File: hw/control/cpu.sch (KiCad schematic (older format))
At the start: 22 parts, among them J301 Conn_02x05_Odd_Even, J302 Conn_01x04, J303 Raspberry_Pi_0_2_3, J304 Micro_SD_Card, J305 Conn_01x06, J306 Conn_01x07, SW301 SW_Push

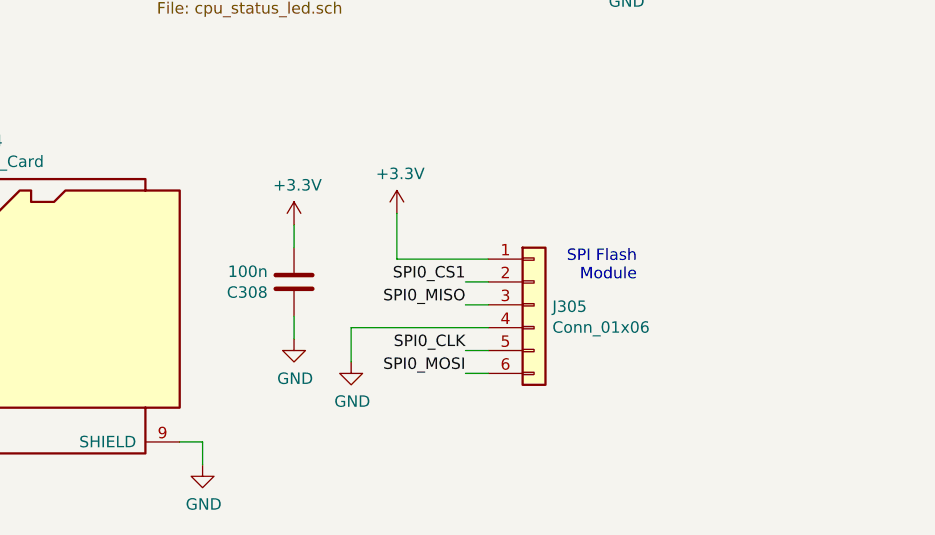
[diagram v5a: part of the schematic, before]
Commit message: [hw] Isolate SD card holder shield from ground
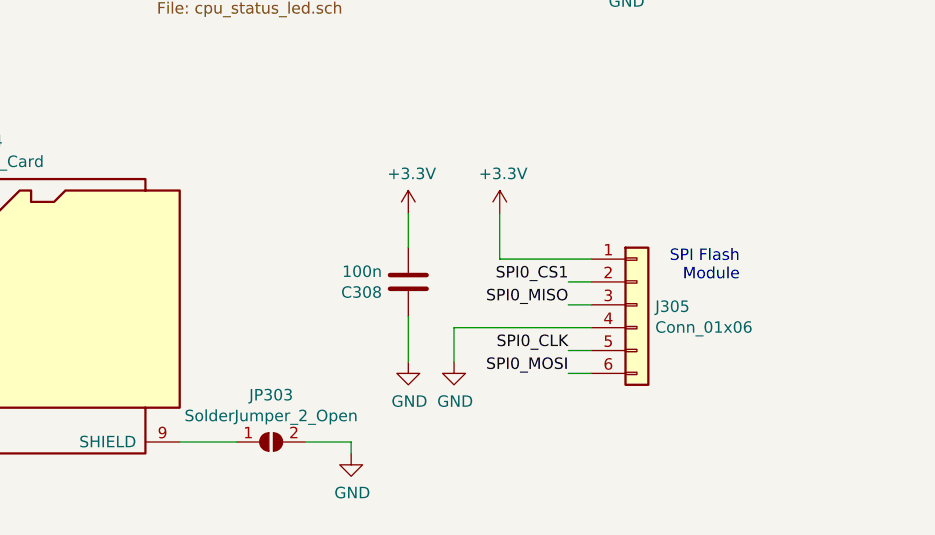
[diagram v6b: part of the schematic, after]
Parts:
- added JP303: SolderJumper_2_Open, Jumper:SolderJumper-2_P1.3mm_Open_RoundedPad1.0x1.5mm, symbol Jumper:SolderJumper_2_Open
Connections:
- net GND: now also JP303.2 (B); no longer J304.9 (SHIELD)
- new net: J304.9 (SHIELD), JP303.1 (A)
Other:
- moved on the sheet: C308, J305
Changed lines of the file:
@@
 L power:GND #PWR0322
 U 1 1 614D2941
-P 4100 7400
-F 0 "#PWR0322" H 4100 7150 50  0001 C CNN
-F 1 "GND" H 4105 7227 50  0000 C CNN
-F 2 "" H 4100 7400 50  0001 C CNN
-F 3 "" H 4100 7400 50  0001 C CNN
-	1    4100 7400
-	1    0    0    -1
-$EndComp
-Wire Wire Line
-	4000 7300 4100 7300
-Wire Wire Line
-	4100 7300 4100 7400
+P 4750 7350
+F 0 "#PWR0322" H 4750 7100 50  0001 C CNN
+F 1 "GND" H 4755 7177 50  0000 C CNN
+F 2 "" H 4750 7350 50  0001 C CNN
+F 3 "" H 4750 7350 50  0001 C CNN
+	1    4750 7350
+	1    0    0    -1
+$EndComp
 $Comp
 L Device:C C302
@@
 L power:+3.3V #PWR0317
 U 1 1 6164D788
-P 4950 6300
-F 0 "#PWR0317" H 4950 6150 50  0001 C CNN
-F 1 "+3.3V" H 4965 6473 50  0000 C CNN
-F 2 "" H 4950 6300 50  0001 C CNN
-F 3 "" H 4950 6300 50  0001 C CNN
-	1    4950 6300
-	1    0    0    -1
-$EndComp
-Wire Wire Line
-	4950 6300 4950 6500
-Wire Wire Line
-	4950 6500 5350 6500
+P 5400 6300
+F 0 "#PWR0317" H 5400 6150 50  0001 C CNN
+F 1 "+3.3V" H 5415 6473 50  0000 C CNN
+F 2 "" H 5400 6300 50  0001 C CNN
+F 3 "" H 5400 6300 50  0001 C CNN
+	1    5400 6300
+	1    0    0    -1
+$EndComp
+Wire Wire Line
+	5400 6300 5400 6500
+Wire Wire Line
+	5400 6500 5800 6500
 $Comp
 L power:GND #PWR0320
 U 1 1 6166C611
-P 4750 6950
-F 0 "#PWR0320" H 4750 6700 50  0001 C CNN
-F 1 "GND" H 4755 6777 50  0000 C CNN
-F 2 "" H 4750 6950 50  0001 C CNN
-F 3 "" H 4750 6950 50  0001 C CNN
-	1    4750 6950
-	1    0    0    -1
-$EndComp
-Wire Wire Line
-	4750 6800 5350 6800
-Text Label 5250 6600 2    50   ~ 0
+P 5200 6950
+F 0 "#PWR0320" H 5200 6700 50  0001 C CNN
+F 1 "GND" H 5205 6777 50  0000 C CNN
+F 2 "" H 5200 6950 50  0001 C CNN
+F 3 "" H 5200 6950 50  0001 C CNN
+	1    5200 6950
+	1    0    0    -1
+$EndComp
+Wire Wire Line
+	5200 6800 5800 6800
+Text Label 5700 6600 2    50   ~ 0
 SPI0_CS1
-Text Label 5250 6700 2    50   ~ 0
+Text Label 5700 6700 2    50   ~ 0
 SPI0_MISO
 Wire Wire Line
-	5250 6600 5350 6600
-Wire Wire Line
-	5250 6700 5350 6700
-Text Label 5250 7000 2    50   ~ 0
+	5700 6600 5800 6600
+Wire Wire Line
+	5700 6700 5800 6700
+Text Label 5700 7000 2    50   ~ 0
 SPI0_MOSI
 Wire Wire Line
-	5250 7000 5350 7000
-Text Label 5250 6900 2    50   ~ 0
+	5700 7000 5800 7000
+Text Label 5700 6900 2    50   ~ 0
 SPI0_CLK
 Wire Wire Line
-	5250 6900 5350 6900
+	5700 6900 5800 6900
 Text Label 5050 2300 0    50   ~ 0
 UART_TXD
@@
 L Connector_Generic:Conn_01x06 J305
 U 1 1 61801594
-P 5550 6700
-F 0 "J305" H 5630 6692 50  0000 L CNN
-F 1 "Conn_01x06" H 5630 6601 50  0000 L CNN
-F 2 "Connector_PinHeader_2.54mm:PinHeader_1x06_P2.54mm_Vertical" H 5550 6700 50  0001 C CNN
-F 3 "~" H 5550 6700 50  0001 C CNN
-	1    5550 6700
-	1    0    0    -1
-$EndComp
-Wire Wire Line
-	4750 6950 4750 6800
+P 6000 6700
+F 0 "J305" H 6080 6692 50  0000 L CNN
+F 1 "Conn_01x06" H 6080 6601 50  0000 L CNN
+F 2 "Connector_PinHeader_2.54mm:PinHeader_1x06_P2.54mm_Vertical" H 6000 6700 50  0001 C CNN
+F 3 "~" H 6000 6700 50  0001 C CNN
+	1    6000 6700
+	1    0    0    -1
+$EndComp
+Wire Wire Line
+	5200 6950 5200 6800
 Text Label 7450 3050 0    50   ~ 0
 IIC0_SDA
@@
 Text Notes 9450 1050 0    50   ~ 0
 RPi RTC connector
-Text Notes 6000 6600 2    50   ~ 0
+Text Notes 6450 6600 2    50   ~ 0
 SPI Flash\nModule
 $Comp
@@
 L Device:C C308
 U 1 1 61666109
-P 4500 6600
-F 0 "C308" H 4615 6646 50  0000 L CNN
-F 1 "100n" H 4615 6555 50  0000 L CNN
-F 2 "Capacitor_SMD:C_0805_2012Metric_Pad1.18x1.45mm_HandSolder" H 4538 6450 50  0001 C CNN
-F 3 "~" H 4500 6600 50  0001 C CNN
-	1    4500 6600
+P 5000 6600
+F 0 "C308" H 5115 6646 50  0000 L CNN
+F 1 "100n" H 5115 6555 50  0000 L CNN
+F 2 "Capacitor_SMD:C_0805_2012Metric_Pad1.18x1.45mm_HandSolder" H 5038 6450 50  0001 C CNN
+F 3 "~" H 5000 6600 50  0001 C CNN
+	1    5000 6600
 	-1   0    0    1
 $EndComp
@@
 L power:GND #PWR0319
 U 1 1 6168F7F5
-P 4500 6850
-F 0 "#PWR0319" H 4500 6600 50  0001 C CNN
-F 1 "GND" H 4505 6677 50  0000 C CNN
-F 2 "" H 4500 6850 50  0001 C CNN
-F 3 "" H 4500 6850 50  0001 C CNN
-	1    4500 6850
+P 5000 6950
+F 0 "#PWR0319" H 5000 6700 50  0001 C CNN
+F 1 "GND" H 5005 6777 50  0000 C CNN
+F 2 "" H 5000 6950 50  0001 C CNN
+F 3 "" H 5000 6950 50  0001 C CNN
+	1    5000 6950
 	1    0    0    -1
 $EndComp
@@
 L power:+3.3V #PWR0318
 U 1 1 6169033D
-P 4500 6350
-F 0 "#PWR0318" H 4500 6200 50  0001 C CNN
-F 1 "+3.3V" H 4515 6523 50  0000 C CNN
-F 2 "" H 4500 6350 50  0001 C CNN
-F 3 "" H 4500 6350 50  0001 C CNN
-	1    4500 6350
-	1    0    0    -1
-$EndComp
-Wire Wire Line
-	4500 6350 4500 6450
-Wire Wire Line
-	4500 6750 4500 6850
+P 5000 6300
+F 0 "#PWR0318" H 5000 6150 50  0001 C CNN
+F 1 "+3.3V" H 5015 6473 50  0000 C CNN
+F 2 "" H 5000 6300 50  0001 C CNN
+F 3 "" H 5000 6300 50  0001 C CNN
+	1    5000 6300
+	1    0    0    -1
+$EndComp
+Wire Wire Line
+	5000 6300 5000 6450
+Wire Wire Line
+	5000 6750 5000 6950
 $Comp
 L power:+3.3V #PWR0305
@@
 Wire Wire Line
 	9000 3550 9000 3650
+Wire Wire Line
+	4000 7300 4250 7300
+Wire Wire Line
+	4550 7300 4750 7300
+Wire Wire Line
+	4750 7300 4750 7350
+$Comp
+L Jumper:SolderJumper_2_Open JP303
+U 1 1 6188626D
+P 4400 7300
+F 0 "JP303" H 4400 7505 50  0000 C CNN
+F 1 "SolderJumper_2_Open" H 4400 7414 50  0000 C CNN
+F 2 "Jumper:SolderJumper-2_P1.3mm_Open_RoundedPad1.0x1.5mm" H 4400 7300 50  0001 C CNN
+F 3 "~" H 4400 7300 50  0001 C CNN
+	1    4400 7300
+	1    0    0    -1
+$EndComp
 $EndSCHEMATC

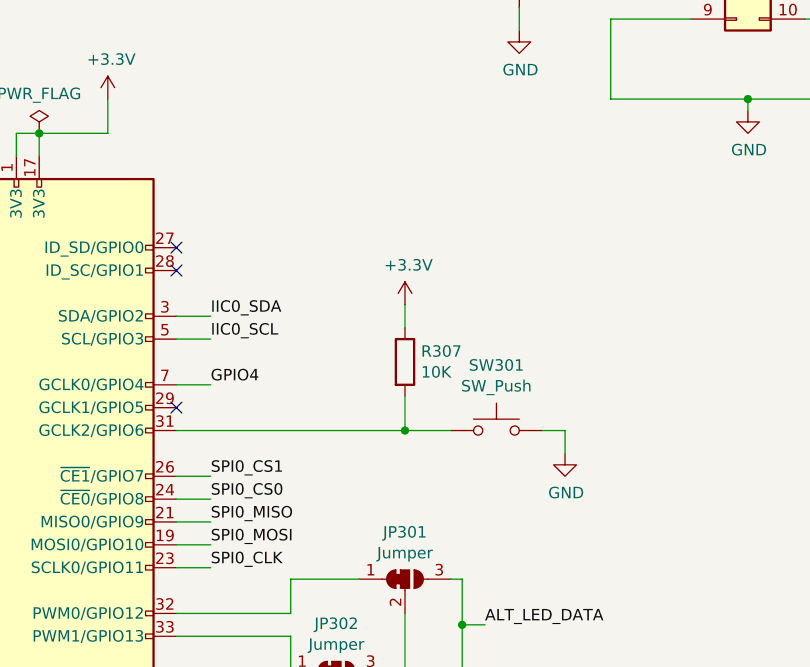
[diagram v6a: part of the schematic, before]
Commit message: [hw] Add HW switch debounce filter
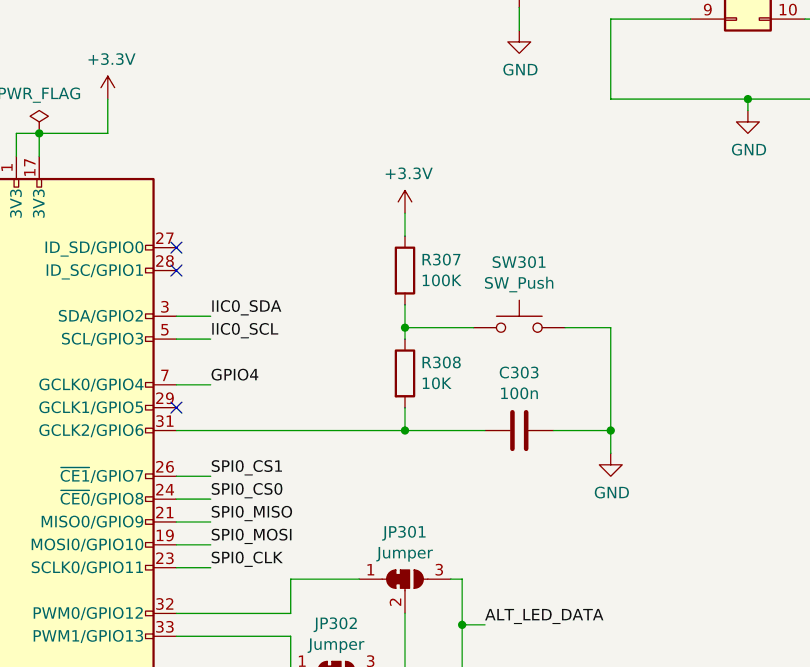
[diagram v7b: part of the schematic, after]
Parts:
- added C303: 100n, Capacitor_SMD:C_0805_2012Metric_Pad1.18x1.45mm_HandSolder, symbol Device:C
- added R308: 10K, Resistor_SMD:R_0805_2012Metric_Pad1.20x1.40mm_HandSolder, symbol Device:R
- R307: value 10K -> 100K
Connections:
- net GND: now also C303.1
- net at R307.2, SW301.1: now also R308.1; no longer J303.31 (GCLK2/GPIO6)
- new net: C303.2, J303.31 (GCLK2/GPIO6), R308.2
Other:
- moved on the sheet: R307, SW301
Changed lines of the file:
@@
 L Switch:SW_Push SW301
 U 1 1 618C6A0D
-P 8700 3550
-F 0 "SW301" H 8700 3835 50  0000 C CNN
-F 1 "SW_Push" H 8700 3744 50  0000 C CNN
-F 2 "Button_Switch_THT:SW_PUSH_6mm" H 8700 3750 50  0001 C CNN
-F 3 "~" H 8700 3750 50  0001 C CNN
-	1    8700 3550
+P 8800 3100
+F 0 "SW301" H 8800 3385 50  0000 C CNN
+F 1 "SW_Push" H 8800 3294 50  0000 C CNN
+F 2 "Button_Switch_THT:SW_PUSH_6mm" H 8800 3300 50  0001 C CNN
+F 3 "~" H 8800 3300 50  0001 C CNN
+	1    8800 3100
 	1    0    0    -1
 $EndComp
@@
 L power:+3.3V #PWR0325
 U 1 1 618C7D00
-P 8300 3000
-F 0 "#PWR0325" H 8300 2850 50  0001 C CNN
-F 1 "+3.3V" H 8315 3173 50  0000 C CNN
-F 2 "" H 8300 3000 50  0001 C CNN
-F 3 "" H 8300 3000 50  0001 C CNN
-	1    8300 3000
-	1    0    0    -1
-$EndComp
-$Comp
-L Device:R R307
-U 1 1 618C8EC8
-P 8300 3250
-F 0 "R307" H 8370 3296 50  0000 L CNN
-F 1 "10K" H 8370 3205 50  0000 L CNN
-F 2 "Resistor_SMD:R_0805_2012Metric_Pad1.20x1.40mm_HandSolder" V 8230 3250 50  0001 C CNN
-F 3 "~" H 8300 3250 50  0001 C CNN
-	1    8300 3250
+P 8300 2600
+F 0 "#PWR0325" H 8300 2450 50  0001 C CNN
+F 1 "+3.3V" H 8315 2773 50  0000 C CNN
+F 2 "" H 8300 2600 50  0001 C CNN
+F 3 "" H 8300 2600 50  0001 C CNN
+	1    8300 2600
 	1    0    0    -1
 $EndComp
 Wire Wire Line
+	8300 2600 8300 2700
+Wire Wire Line
 	8300 3000 8300 3100
-Wire Wire Line
-	8300 3400 8300 3550
-Wire Wire Line
-	8300 3550 8500 3550
-Wire Wire Line
-	7300 3550 8300 3550
-Connection ~ 8300 3550
 $Comp
 L power:GND #PWR0326
 U 1 1 618F59EF
-P 9000 3650
-F 0 "#PWR0326" H 9000 3400 50  0001 C CNN
-F 1 "GND" H 9005 3477 50  0000 C CNN
-F 2 "" H 9000 3650 50  0001 C CNN
-F 3 "" H 9000 3650 50  0001 C CNN
-	1    9000 3650
+P 9200 3650
+F 0 "#PWR0326" H 9200 3400 50  0001 C CNN
+F 1 "GND" H 9205 3477 50  0000 C CNN
+F 2 "" H 9200 3650 50  0001 C CNN
+F 3 "" H 9200 3650 50  0001 C CNN
+	1    9200 3650
 	1    0    0    -1
 $EndComp
 Wire Wire Line
-	8900 3550 9000 3550
+	9000 3100 9200 3100
 Wire Wire Line
-	9000 3550 9000 3650
+	9200 3100 9200 3550
 Wire Wire Line
 	4000 7300 4250 7300
@@
 	1    0    0    -1
 $EndComp
+$Comp
+L Device:C C303
+U 1 1 61887BB2
+P 8800 3550
+F 0 "C303" V 8548 3550 50  0000 C CNN
+F 1 "100n" V 8639 3550 50  0000 C CNN
+F 2 "Capacitor_SMD:C_0805_2012Metric_Pad1.18x1.45mm_HandSolder" H 8838 3400 50  0001 C CNN
+F 3 "~" H 8800 3550 50  0001 C CNN
+	1    8800 3550
+	0    1    1    0
+$EndComp
+Wire Wire Line
+	8950 3550 9200 3550
+Connection ~ 9200 3550
+Wire Wire Line
+	9200 3550 9200 3650
+Wire Wire Line
+	8300 3550 8650 3550
+Wire Wire Line
+	8300 3450 8300 3550
+Wire Wire Line
+	8600 3100 8300 3100
+Connection ~ 8300 3100
+Wire Wire Line
+	8300 3100 8300 3150
+Wire Wire Line
+	8300 3550 7300 3550
+Connection ~ 8300 3550
+$Comp
+L Device:R R307
+U 1 1 618C8EC8
+P 8300 2850
+F 0 "R307" H 8370 2896 50  0000 L CNN
+F 1 "100K" H 8370 2805 50  0000 L CNN
+F 2 "Resistor_SMD:R_0805_2012Metric_Pad1.20x1.40mm_HandSolder" V 8230 2850 50  0001 C CNN
+F 3 "~" H 8300 2850 50  0001 C CNN
+	1    8300 2850
+	1    0    0    -1
+$EndComp
+$Comp
+L Device:R R308
+U 1 1 6198CE7C
+P 8300 3300
+F 0 "R308" H 8370 3346 50  0000 L CNN
+F 1 "10K" H 8370 3255 50  0000 L CNN
+F 2 "Resistor_SMD:R_0805_2012Metric_Pad1.20x1.40mm_HandSolder" V 8230 3300 50  0001 C CNN
+F 3 "~" H 8300 3300 50  0001 C CNN
+	1    8300 3300
+	1    0    0    -1
+$EndComp

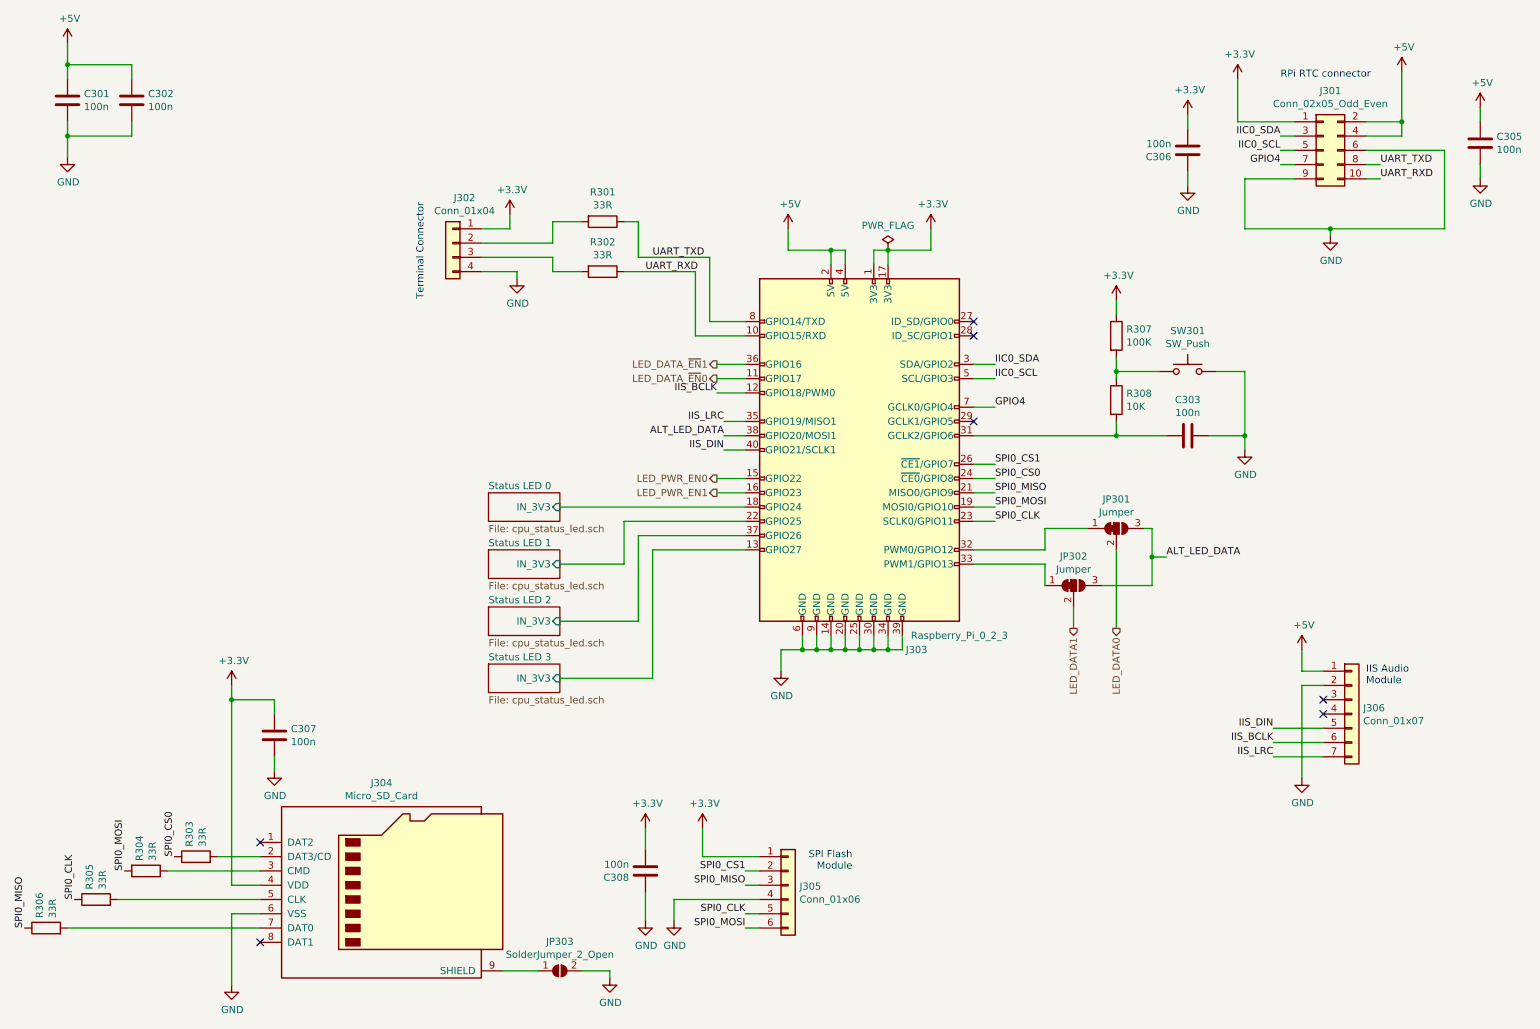
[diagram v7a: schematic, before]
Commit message: [hw] Add ID EEPROM to control board
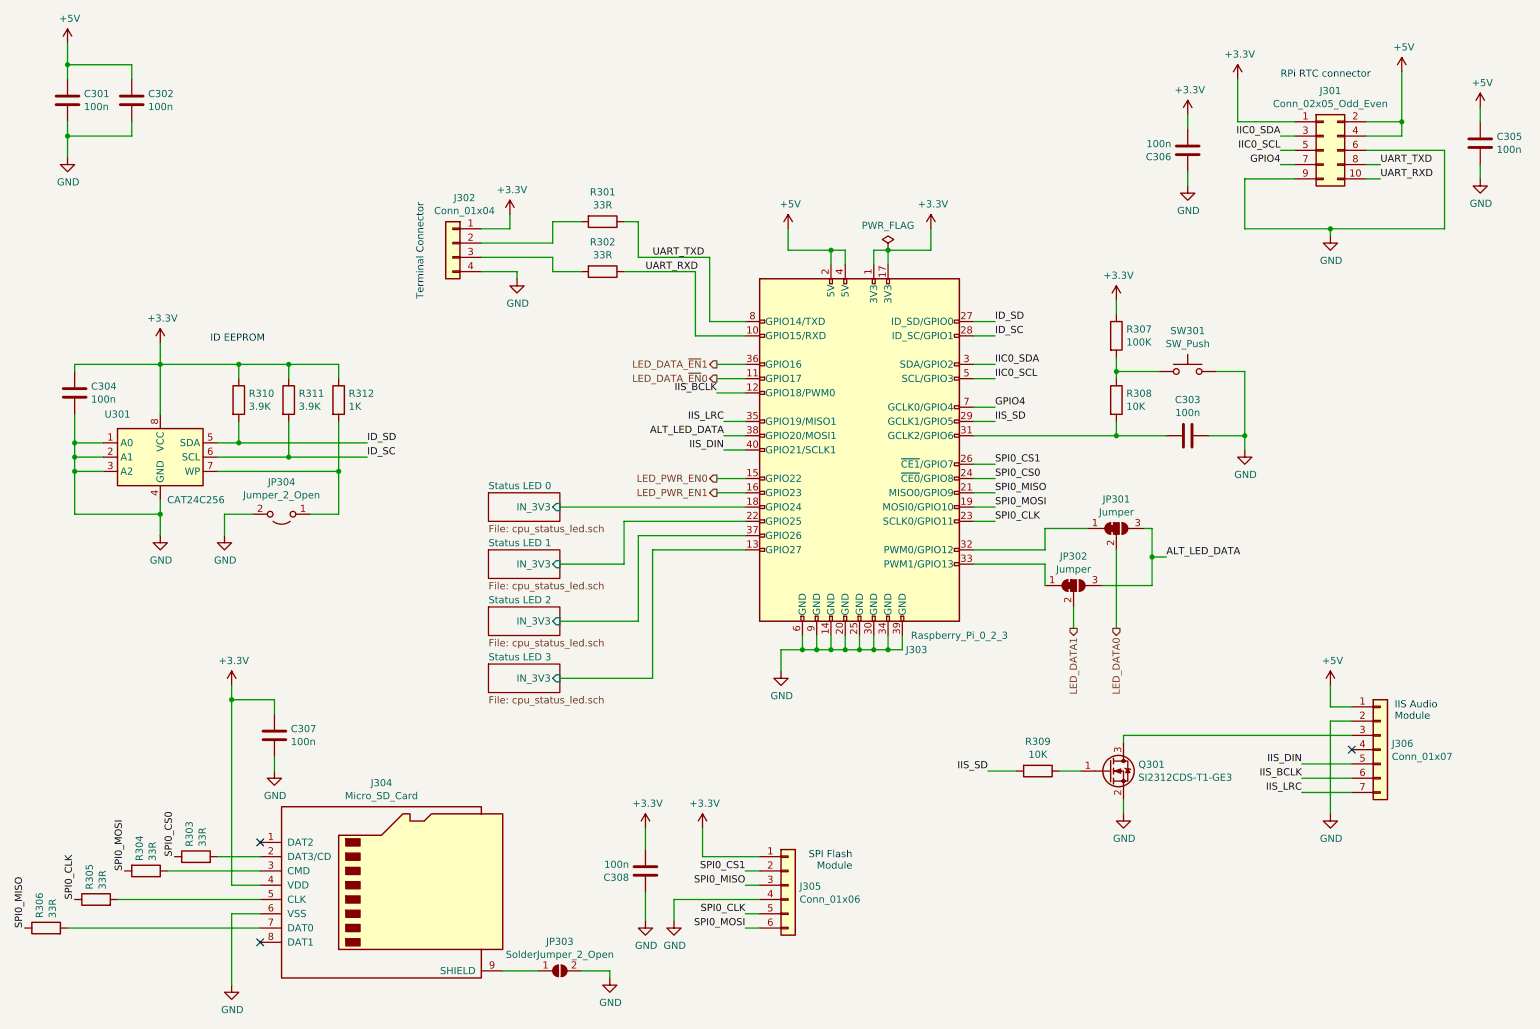
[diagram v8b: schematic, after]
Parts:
- added C304: 100n, Capacitor_SMD:C_0805_2012Metric_Pad1.18x1.45mm_HandSolder, symbol Device:C
- added JP304: Jumper_2_Open, Connector_PinHeader_2.54mm:PinHeader_1x02_P2.54mm_Horizontal, symbol Jumper:Jumper_2_Open
- added Q301: SI2312CDS-T1-GE3, Package_TO_SOT_SMD:SOT-23_Handsoldering, symbol Device:Q_NMOS_GSD
- added R309: 10K, Resistor_SMD:R_0805_2012Metric_Pad1.20x1.40mm_HandSolder, symbol Device:R
- added R310, R311: 3.9K, Resistor_SMD:R_0805_2012Metric_Pad1.20x1.40mm_HandSolder, symbol Device:R
- added R312: 1K, Resistor_SMD:R_0805_2012Metric_Pad1.20x1.40mm_HandSolder, symbol Device:R
- added U301: CAT24C256, Package_SO:SOIC-8_3.9x4.9mm_P1.27mm, symbol Memory_EEPROM:CAT24C256
- J305: footprint Connector_PinHeader_2.54mm:PinHeader_1x06_P2.54mm_Vertical -> Connector_PinSocket_2.54mm:PinSocket_1x06_P2.54mm_Vertical
- J306: footprint Connector_PinHeader_2.54mm:PinHeader_1x07_P2.54mm_Vertical -> Connector_PinSocket_2.54mm:PinSocket_1x07_P2.54mm_Vertical
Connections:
- net +3V3: now also C304.1, R310.1, R311.1, R312.1, U301.8 (VCC)
- net GND: now also C304.2, JP304.2 (B), Q301.2 (S), U301.1 (A0), U301.2 (A1), U301.3 (A2), U301.4 (GND)
- net ID_SD: now reaches J303.27 (ID_SD/GPIO0)
- net ID_SD: now also R310.2, U301.5 (SDA)
- net ID_SC: now reaches J303.28 (ID_SC/GPIO1)
- net ID_SC: now also R311.2, U301.6 (SCL)
- net IIS_SD: now reaches J303.29 (GCLK1/GPIO5)
- net IIS_SD: now also R309.2
- net at J306.3 (Pin_3): now also Q301.3 (D)
- new net: Q301.1 (G), R309.1
- new net: JP304.1 (A), R312.2, U301.7 (WP)
- no-connect marks 7 -> 3
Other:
- note added: "ID EEPROM"
- moved on the sheet: J306
